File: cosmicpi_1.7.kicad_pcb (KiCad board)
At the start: 4 copper layers, 128 x 184 mm, 231 parts, among them J1 Barrel_Jack_Switch, J10 Conn_01x02_Female, J11 Conn_01x02_Male, J12 Conn_01x02_Male, J13 Conn_01x02_Female, J14 Conn_01x02_Male, J15 Conn_01x02_Female, J2 SMA, J3 USB_B_Micro, J4 Conn_01x04_Male, J5 Conn_01x04_Male, J6 SWD, J7 Raspberry_Pi_2_3, J8 Conn_01x02_Male, J9 Conn_01x02_Female, Q1 BSS123, Q2 BSS123, U1 MCP47CMB22, U10 TPS62163DSG, U11 LM555, U12 LM555, U13 LP2985-3.3, U14 AD8039, U15 AD8039, U16 LP2985-3.3, U17 MAX1932, U18 MAX1932, U19 AD8039, U2 STM32F401RETx, U3 L76-M33, U4 74HC00, U5 BME280, U5 LPS25HB, U6 LM555, U7 LSM9DS1, U8 SI7006-A20, U9 MAX991, Y1 8 MHz

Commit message: updated a little
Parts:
- removed the REF** at (103.0, 56.0)
- removed the REF** at (56.5, 30.0)
- removed the REF** at (20.2, 69.2)
- removed the REF** at (100.0, 91.2)
- removed the REF** at (78.8, 119.2)
- removed the REF** at (70.0, 99.8)
- removed the REF** at (20.5, 156.0)
- removed the REF** at (141.2, 109.2)
- removed the REF** at (128.5, 118.5)
- removed the REF** at (44.2, 26.0)
- removed the REF** at (139.8, 39.0)
- removed the REF** at (103.0, 167.0)
- removed the REF** at (82.8, 55.0)
- removed the REF** at (46.8, 54.0)
- removed the REF** at (18.8, 20.2)
- removed the REF** at (100.0, 75.5)
- removed the REF** at (100.0, 144.5)
- removed the REF** at (46.8, 75.5)
- removed the REF** at (33.8, 75.5)
- removed the REF** at (85.5, 168.5)
- removed the REF** at (57.5, 168.5)
- removed the U5 at (49.5, 23.0)
- added C100: 10u, Capacitor_SMD:C_1206_3216Metric, F.Cu at (-70.3, 109.9)
- added C101: 10u, Capacitor_SMD:C_1206_3216Metric, F.Cu at (-47.9, 90.2)
- added C102: 10u, Capacitor_SMD:C_1206_3216Metric, F.Cu at (-64.7, 106.7)
- added C103: 10u, Capacitor_SMD:C_1206_3216Metric, F.Cu at (-59.1, 100.1)
- added C104: 10u, Capacitor_SMD:C_1206_3216Metric, F.Cu at (-53.5, 96.8)
- added C105: 10u, Capacitor_SMD:C_1206_3216Metric, F.Cu at (-47.9, 93.5)
- added C106: 10u, Capacitor_SMD:C_1206_3216Metric, F.Cu at (-59.1, 103.4)
- added C107: 10u, Capacitor_SMD:C_1206_3216Metric, F.Cu at (-64.7, 109.9)
- added C108: 10u, Capacitor_SMD:C_1206_3216Metric, F.Cu at (-42.3, 90.2)
- added C109: 10u, Capacitor_SMD:C_1206_3216Metric, F.Cu at (-59.1, 106.7)
- added C110: 10u, Capacitor_SMD:C_1206_3216Metric, F.Cu at (-53.5, 100.1)
- added C111: 10n, Capacitor_SMD:C_1206_3216Metric, F.Cu at (-42.3, 93.5)
- added C77: 4.3p, Capacitor_SMD:C_0603_1608Metric, F.Cu at (-37.3, 64.8)
- added C78: 4.3p, Capacitor_SMD:C_0603_1608Metric, F.Cu at (-43.9, 66.5)
- added C79: 100n, Capacitor_SMD:C_0603_1608Metric, F.Cu at (-48.0, 71.0)
- added C80: 10u, Capacitor_SMD:C_1206_3216Metric, F.Cu at (-59.1, 109.9)
- added C81: 10u, Capacitor_SMD:C_1206_3216Metric, F.Cu at (-53.5, 103.4)
- added C82: 10u, Capacitor_SMD:C_1206_3216Metric, F.Cu at (-36.7, 90.2)
- added C83: 10u, Capacitor_SMD:C_1206_3216Metric, F.Cu at (-59.1, 96.8)
- added C84: 10u, Capacitor_SMD:C_1206_3216Metric, F.Cu at (-53.5, 93.5)
- added C85: 10u, Capacitor_SMD:C_1206_3216Metric, F.Cu at (-70.3, 93.5)
- added C86: 10u, Capacitor_SMD:C_1206_3216Metric, F.Cu at (-64.7, 90.2)
- added C87: 10u, Capacitor_SMD:C_1206_3216Metric, F.Cu at (-70.3, 96.8)
- added C88: 10u, Capacitor_SMD:C_1206_3216Metric, F.Cu at (-64.7, 93.5)
- added C89: 10u, Capacitor_SMD:C_1206_3216Metric, F.Cu at (-59.1, 90.2)
- added C90: 10u, Capacitor_SMD:C_1206_3216Metric, F.Cu at (-70.3, 100.1)
- added C91: 10u, Capacitor_SMD:C_1206_3216Metric, F.Cu at (-64.7, 96.8)
- added C92: 10u, Capacitor_SMD:C_1206_3216Metric, F.Cu at (-59.1, 93.5)
- added C93: 10u, Capacitor_SMD:C_1206_3216Metric, F.Cu at (-70.3, 103.4)
- added C94: 10u, Capacitor_SMD:C_1206_3216Metric, F.Cu at (-53.5, 90.2)
- added C95: 10n, Capacitor_SMD:C_1206_3216Metric, F.Cu at (-70.3, 106.7)
- added C96: 10u, Capacitor_SMD:C_1206_3216Metric, F.Cu at (-64.7, 100.1)
- added C97: 10u, Capacitor_SMD:C_1206_3216Metric, F.Cu at (-47.9, 96.8)
- added C98: 10u, Capacitor_SMD:C_1206_3216Metric, F.Cu at (-70.3, 90.2)
- added C99: 10u, Capacitor_SMD:C_1206_3216Metric, F.Cu at (-64.7, 103.4)
- added D10: B140, Diode_SMD:D_SMA, F.Cu at (-50.0, 67.5)
- added D11: BAT54SW, Package_TO_SOT_SMD:SOT-323_SC-70, F.Cu at (-37.3, 93.7)
- added D12: BAT54SW, Package_TO_SOT_SMD:SOT-323_SC-70, F.Cu at (-48.5, 104.8)
- added D13: BAT54SW, Package_TO_SOT_SMD:SOT-323_SC-70, F.Cu at (-31.6, 90.4)
- added D14: BAT54SW, Package_TO_SOT_SMD:SOT-323_SC-70, F.Cu at (-44.0, 100.6)
- added D15: BAT54SW, Package_TO_SOT_SMD:SOT-323_SC-70, F.Cu at (-54.1, 111.4)
- added D16: BAT54SW, Package_TO_SOT_SMD:SOT-323_SC-70, F.Cu at (-38.4, 97.3)
- added D17: BAT54SW, Package_TO_SOT_SMD:SOT-323_SC-70, F.Cu at (-49.6, 108.5)
- added D18: BAT54SW, Package_TO_SOT_SMD:SOT-323_SC-70, F.Cu at (-44.0, 104.3)
- added D19: BAT54SW, Package_TO_SOT_SMD:SOT-323_SC-70, F.Cu at (-32.8, 94.0)
- added D20: BAT54SW, Package_TO_SOT_SMD:SOT-323_SC-70, F.Cu at (-42.9, 97.0)
- added D21: BAT54SW, Package_TO_SOT_SMD:SOT-323_SC-70, F.Cu at (-39.6, 101.0)
- added D22: BAT54SW, Package_TO_SOT_SMD:SOT-323_SC-70, F.Cu at (-45.2, 108.5)
- added D23: BAT54SW, Package_TO_SOT_SMD:SOT-323_SC-70, F.Cu at (-34.0, 97.7)
- added D24: BAT54SW, Package_TO_SOT_SMD:SOT-323_SC-70, F.Cu at (-39.6, 104.6)
- added D9: B140, Diode_SMD:D_SMA, F.Cu at (-35.3, 61.2)
- added Q3: BSS123, Package_TO_SOT_SMD:SOT-23, F.Cu at (-48.5, 100.7)
- added Q4: BSS123, Package_TO_SOT_SMD:SOT-23, F.Cu at (-54.1, 107.3)
- added R71: 100k, Resistor_SMD:R_0603_1608Metric, F.Cu at (-52.0, 71.0)
- added R72: 10k, Resistor_SMD:R_0603_1608Metric, F.Cu at (-41.0, 107.7)
- added R73: 180, Resistor_SMD:R_0603_1608Metric, F.Cu at (-35.3, 100.8)
- added R74: 10k, Resistor_SMD:R_0603_1608Metric, F.Cu at (-41.8, 111.5)
- added R75: 10k, Resistor_SMD:R_0603_1608Metric, F.Cu at (-49.9, 111.5)
- added R76: 180, Resistor_SMD:R_0603_1608Metric, F.Cu at (-45.8, 111.5)
- added R77: 10k, Resistor_SMD:R_0603_1608Metric, F.Cu at (-35.3, 103.3)
- added Y2: 32.768KHz, Crystal:Crystal_SMD_HC49-SD, F.Cu at (-46.7, 62.1)
- C56: value 10u -> 470u; footprint Capacitor_SMD:C_0603_1608Metric -> Capacitor_SMD:C_Elec_10x10.2
- U8: value SI7006-A20 -> ESP-12F; footprint Package_DFN_QFN:DFN-6-1EP_3x3mm_P1mm_EP1.5x2.4mm -> RF_Module:ESP-12E
- moved U8 177.6 mm to (109.2, 185.4), turned to 180 degrees
- moved J7 146.4 mm to (69.8, 172.7)
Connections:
- C43 pad 1: V_OFFSET -> GNDREF
- C43 pad 2: GNDREF -> V_OFFSET
- C44 pad 1: V_OFFSET -> GNDREF
- C44 pad 2: GNDREF -> V_OFFSET
- C49 pad 1: V_OFFSET -> GNDREF
- C49 pad 2: GNDREF -> V_OFFSET
- C50 pad 1: V_OFFSET -> GNDREF
- C50 pad 2: GNDREF -> V_OFFSET
- C56 pad 1: GND -> Net-(C56-Pad1)
- C56 pad 2: Net-(C56-Pad2) -> GND
- J1 pad 1: Net-(C56-Pad2) -> Net-(D9-Pad1)
- J3 pad 1: USB_OTG_VBUS -> Net-(D10-Pad1)
- J7 pad 3: SDA_SLAVE -> ESP_Reset
- J7 pad 5: SCL_SLAVE -> ESP_Boot
- R6 pad 2: LED1 -> pwr_led
- R7 pad 2: LED2 -> evt_led
- U1 pad 6: Net-(U1-Pad6) -> GND
- U10 pad 2: Net-(C56-Pad2) -> Net-(C56-Pad1)
- U10 pad 3: Net-(C56-Pad2) -> Net-(C56-Pad1)
- U2 pad 16: Net-(U2-Pad16) -> GPSRX
- U2 pad 17: Net-(U2-Pad17) -> GPSTX
- U2 pad 20: LED1 -> BIASFB1
- U2 pad 21: LED2 -> BIASFB2
- U2 pad 23: BIASFB1 -> pwr_led
- U2 pad 26: BIASFB2 -> PSU_B_DRIVE
- U2 pad 29: TRIG_OUT -> Net-(U2-Pad29)
- U2 pad 3: ACC_INT1 -> Net-(C77-Pad1)
- U2 pad 4: ACC_INT2 -> Net-(C78-Pad1)
- U2 pad 40: MAG_INT -> Net-(U2-Pad40)
- U2 pad 41: SCL_SLAVE -> evt_led
- U2 pad 55: Net-(U2-Pad55) -> TRIG_OUT
- U2 pad 56: SDA_SLAVE -> Net-(U2-Pad56)
- U2 pad 57: Net-(U2-Pad57) -> PSU_A_DRIVE
- U2 pad 58: GPSRX -> Net-(U2-Pad58)
- U7 pad 10: MAG_INT -> Net-(U7-Pad10)
- U7 pad 11: ACC_INT2 -> Net-(U7-Pad11)
- U7 pad 12: ACC_INT1 -> Net-(U7-Pad12)
- U8 pad 1: SDA0 -> ESP_Reset
- U8 pad 2: GND -> Net-(U8-Pad2)
- U8 pad 3: Net-(U8-Pad3) -> +3V3
- U8 pad 5: +3V3 -> Net-(U8-Pad5)
- U8 pad 6: SCL0 -> Net-(U8-Pad6)
- U8 pad 7: (no net) -> Net-(U8-Pad7)
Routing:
- net +5V: track 373.2 -> 0.00 mm, vias 4 -> 0
- net _RESET: track 178.8 -> 0.00 mm, vias 2 -> 0
- net RX0: track 83.2 -> 0.00 mm, vias 2 -> 0
- net TX0: track 78.7 -> 0.00 mm, vias 2 -> 0
- net FLAG: track 48.0 -> 0.00 mm, vias 3 -> 0
- net SDA_SLAVE: track 43.2 -> 0.00 mm, vias 2 -> 0
- net BOOT0: track 40.2 -> 0.00 mm, vias 2 -> 0
- net SCL_SLAVE: track 36.5 -> 0.00 mm, vias 2 -> 0
- net Net-(U2-Pad2): track 0.00 -> 30.5 mm, vias 0 -> 2
- net BARO_INT: track 30.5 -> 0.00 mm, vias 2 -> 0
- removed copper zone on F.Cu, net (none)
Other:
- board size 128 x 184 mm -> 128 x 231.6 mm

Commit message: footprints corrected, routing in progress
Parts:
- removed C100, C101, C102, C103, C104, C105, C106, C107, C108, C109, C110, C80, C81, C82, C83, C84, C85, C86, C87, C88, C89, C90, C91, C92, C93, C94, C96, C97, C98, C99: 10u, Capacitor_SMD:C_1206_3216Metric
- removed C111, C95: 10n, Capacitor_SMD:C_1206_3216Metric
- removed D11, D12, D13, D14, D15, D16, D17, D18, D19, D20, D21, D22, D23, D24: BAT54SW, Package_TO_SOT_SMD:SOT-323_SC-70
- removed Q3, Q4: BSS123, Package_TO_SOT_SMD:SOT-23
- removed R72, R74, R75, R77: 10k, Resistor_SMD:R_0603_1608Metric
- removed R73, R76: 180, Resistor_SMD:R_0603_1608Metric
- D10, D9: value B140 -> B140-E3
- Y1: footprint Crystal:Crystal_SMD_HC49-SD -> Crystal:Crystal_SMD_5032-4Pin_5.0x3.2mm
- Y2: footprint Crystal:Crystal_SMD_HC49-SD -> Crystal:Crystal_SMD_EuroQuartz_EQ161-2Pin_3.2x1.5mm
- moved R71 206.4 mm to (121.0, 183.6), turned to 180 degrees
- moved C79 204.8 mm to (120.6, 187.4), turned to 90 degrees
- moved Y2 105.5 mm to (56.4, 39.8), turned to 270 degrees
- moved C78 100.4 mm to (53.2, 41.0), turned to 180 degrees
- moved C77 94.3 mm to (53.2, 38.4), turned to 180 degrees
- moved D10 84.8 mm to (23.6, 109.6), turned to 90 degrees
- moved D9 63.5 mm to (27.6, 70.0), turned to 180 degrees
- moved U5 37.5 mm to (35.6, 22.6)
- moved C15 21.4 mm to (32.6, 21.2)
- moved C57 11.5 mm to (35.2, 99.6)
- moved U16 10.6 mm to (29.6, 87.6)
- moved C58 10.3 mm to (32.8, 91.2)
- moved U10 9.92 mm to (32.9, 96.2)
- moved L1 8.96 mm to (36.6, 96.6)
- moved C3 8.34 mm to (53.4, 44.2)
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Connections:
- D10 pad 1: Net-(D10-Pad1) -> Net-(C56-Pad1)
- D10 pad 2: +5V -> Net-(D10-Pad2)
- D9 pad 1: Net-(D9-Pad1) -> +5V
- D9 pad 2: Net-(C56-Pad1) -> Net-(D9-Pad2)
- J1 pad 1: Net-(D9-Pad1) -> Net-(D10-Pad2)
- J3 pad 1: Net-(D10-Pad1) -> Net-(D9-Pad2)
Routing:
- net LED2: track 132.5 -> 0.00 mm, vias 2 -> 0
- net LED1: track 124.6 -> 0.00 mm, vias 2 -> 0
- net SWCLK: track 119.9 -> 0.00 mm, vias 4 -> 0
- net SWDIO: track 118.8 -> 0.00 mm, vias 3 -> 0
- net USB_OTG_DM: track 111.5 -> 0.00 mm, vias 2 -> 0
- net USB_OTG_DP: track 111.1 -> 7.95 mm, vias 3 -> 1
- net USB_OTG_VBUS: track 94.0 -> 0.00 mm, vias 2 -> 0
- net MAG_INT: track 79.6 -> 0.00 mm, vias 4 -> 0
- net HVPSU_CS2: track 59.1 -> 4.87 mm, vias 3 -> 0
- net ACC_INT2: track 45.7 -> 0.00 mm, vias 2 -> 0
- net GND: track 139.2 -> 93.8 mm, vias 135 -> 121
- net ACC_INT1: track 44.6 -> 0.00 mm, vias 2 -> 0
- net Net-(U2-Pad2): track 30.5 -> 0.00 mm, vias 2 -> 0
- net Net-(C4-Pad1): track 15.0 -> 0.00 mm
- net +3V3: track 306.3 -> 291.4 mm, vias 27 -> 28
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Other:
- board size 128 x 231.6 mm -> 128 x 184 mm
- board text added: "<- side LED orientation"
- board text removed: "SCINTILLATOR SUPPORT"

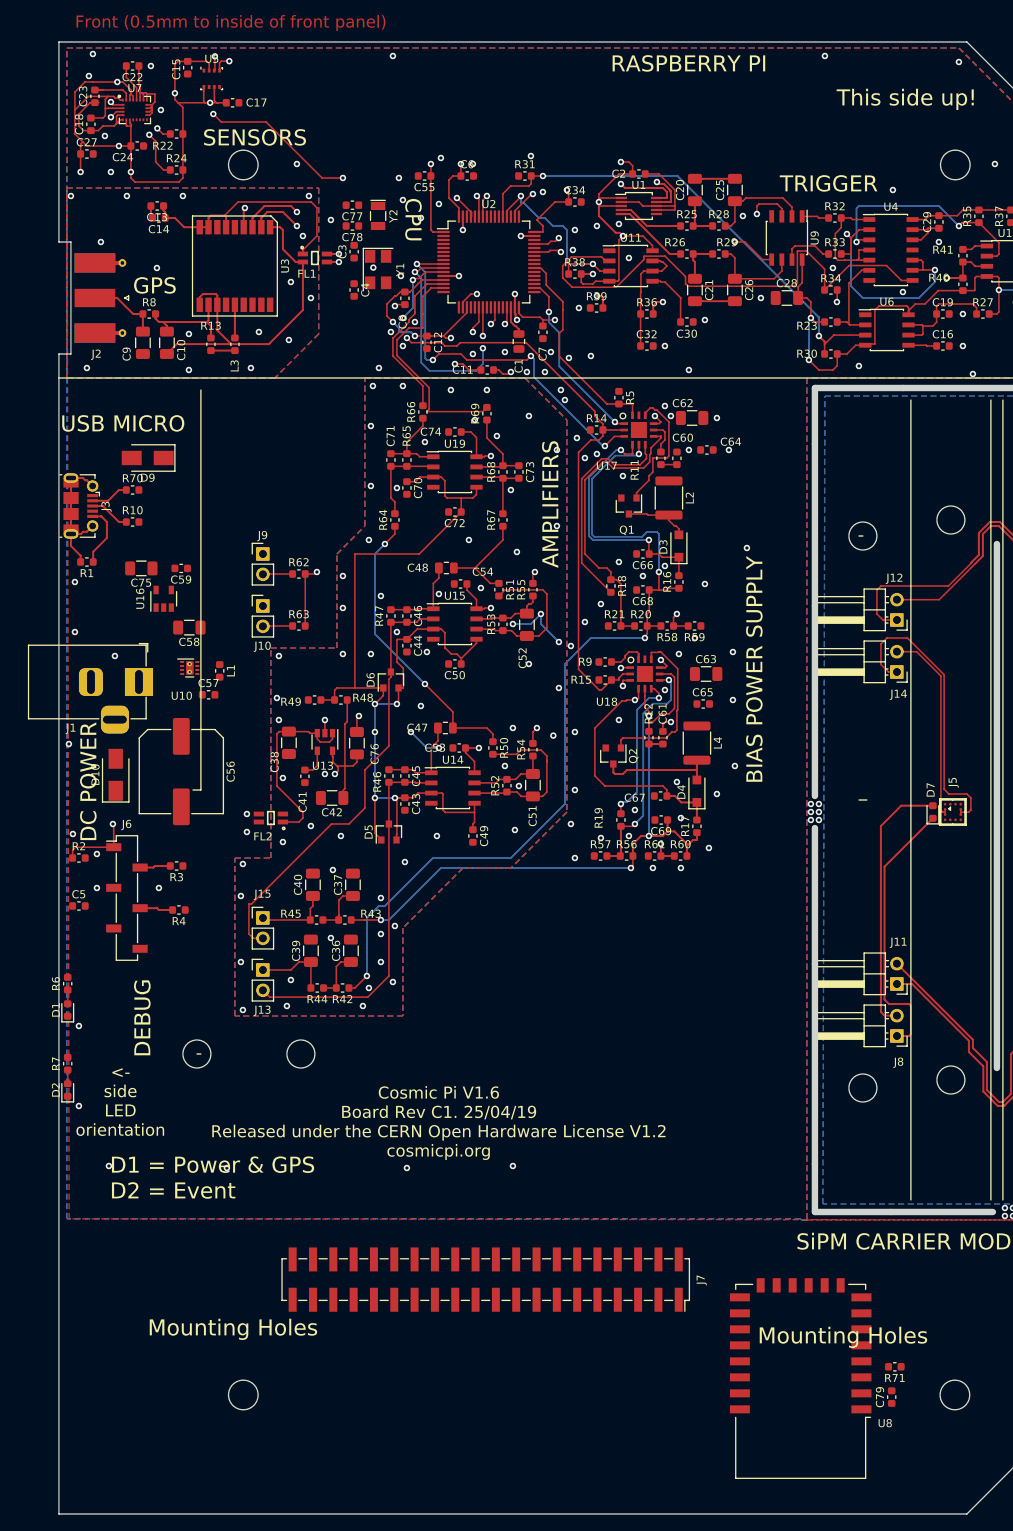
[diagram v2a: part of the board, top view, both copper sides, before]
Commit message: finished place and route
BOM still needs updating!
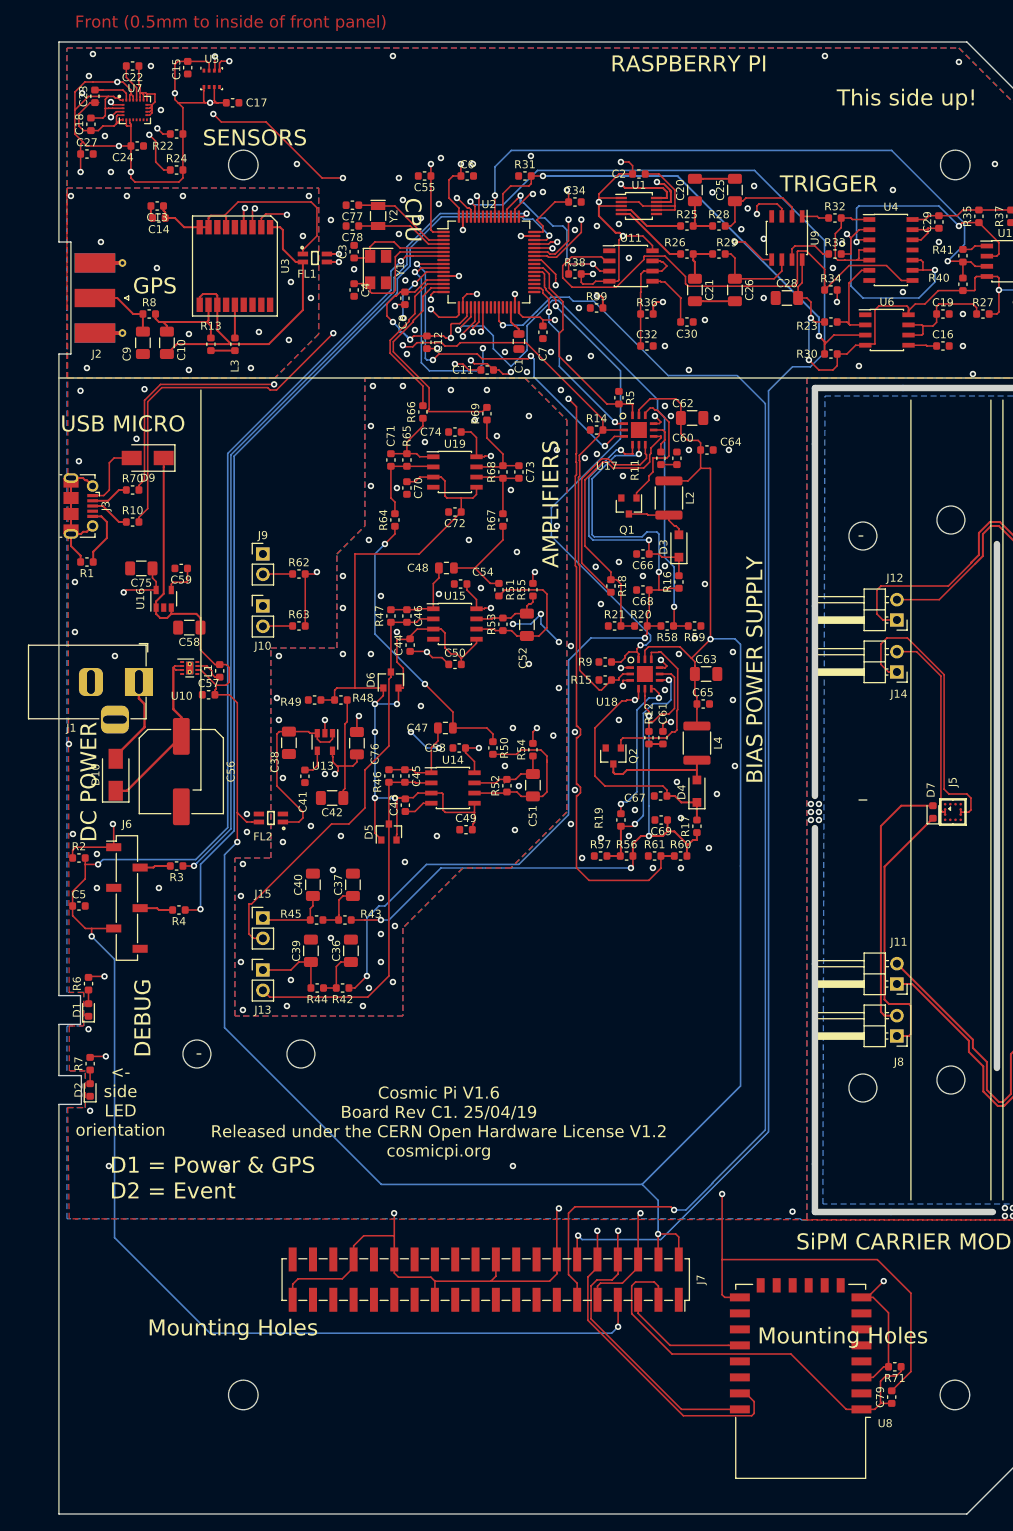
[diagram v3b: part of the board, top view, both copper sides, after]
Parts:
- moved D2 2.80 mm to (20.4, 149.0)
- moved R7 2.80 mm to (20.4, 145.7)
- moved D1 2.60 mm to (20.2, 139.0)
- moved R6 2.60 mm to (20.2, 135.7)
- moved C49 1.17 mm to (67.4, 116.5), turned to 0 degrees
- moved C44 0.41 mm to (60.4, 93.4), turned to 90 degrees
- moved C43 0.16 mm to (59.8, 113.4), turned to 90 degrees
- moved C50 0.05 mm to (66.0, 95.8), turned to 0 degrees
- turned L1 to 90 degrees
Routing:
- net +5V: track 0.00 -> 307.4 mm, vias 0 -> 3
- net _RESET: track 0.00 -> 230.5 mm, vias 0 -> 4
- net TX0: track 0.00 -> 206.3 mm, vias 0 -> 2
- net RX0: track 0.00 -> 201.9 mm, vias 0 -> 2
- net BOOT0: track 0.00 -> 200.2 mm, vias 0 -> 2
- net FLAG: track 0.00 -> 173.5 mm, vias 0 -> 2
- net evt_led: track 0.00 -> 134.6 mm, vias 0 -> 2
- net GND: track 93.8 -> 224.5 mm, vias 121 -> 129
- net pwr_led: track 0.00 -> 118.6 mm, vias 0 -> 2
- net SWDIO: track 0.00 -> 117.7 mm, vias 0 -> 2
- net SWCLK: track 0.00 -> 107.6 mm, vias 0 -> 2
- net USB_OTG_DM: track 0.00 -> 74.6 mm, vias 0 -> 2
- net USB_OTG_DP: track 7.95 -> 80.6 mm, vias 1 -> 2
- net HVPSU_CS2: track 4.87 -> 67.3 mm, vias 0 -> 2
- net ESP_Reset: track 0.00 -> 53.2 mm
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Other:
- outline, holes or cut-outs redrawn

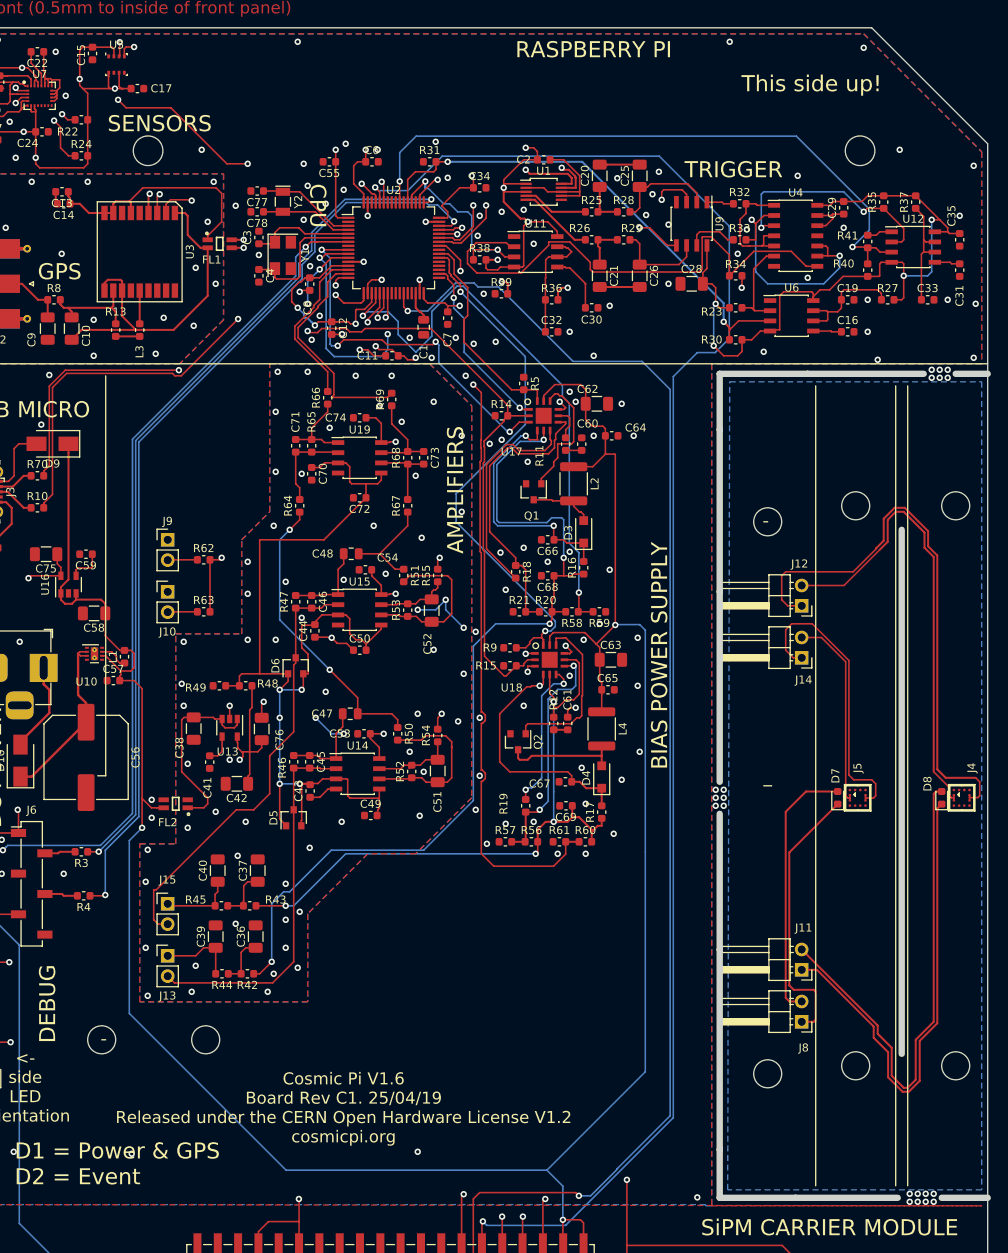
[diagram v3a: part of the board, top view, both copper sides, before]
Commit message: added BOM for 1.7
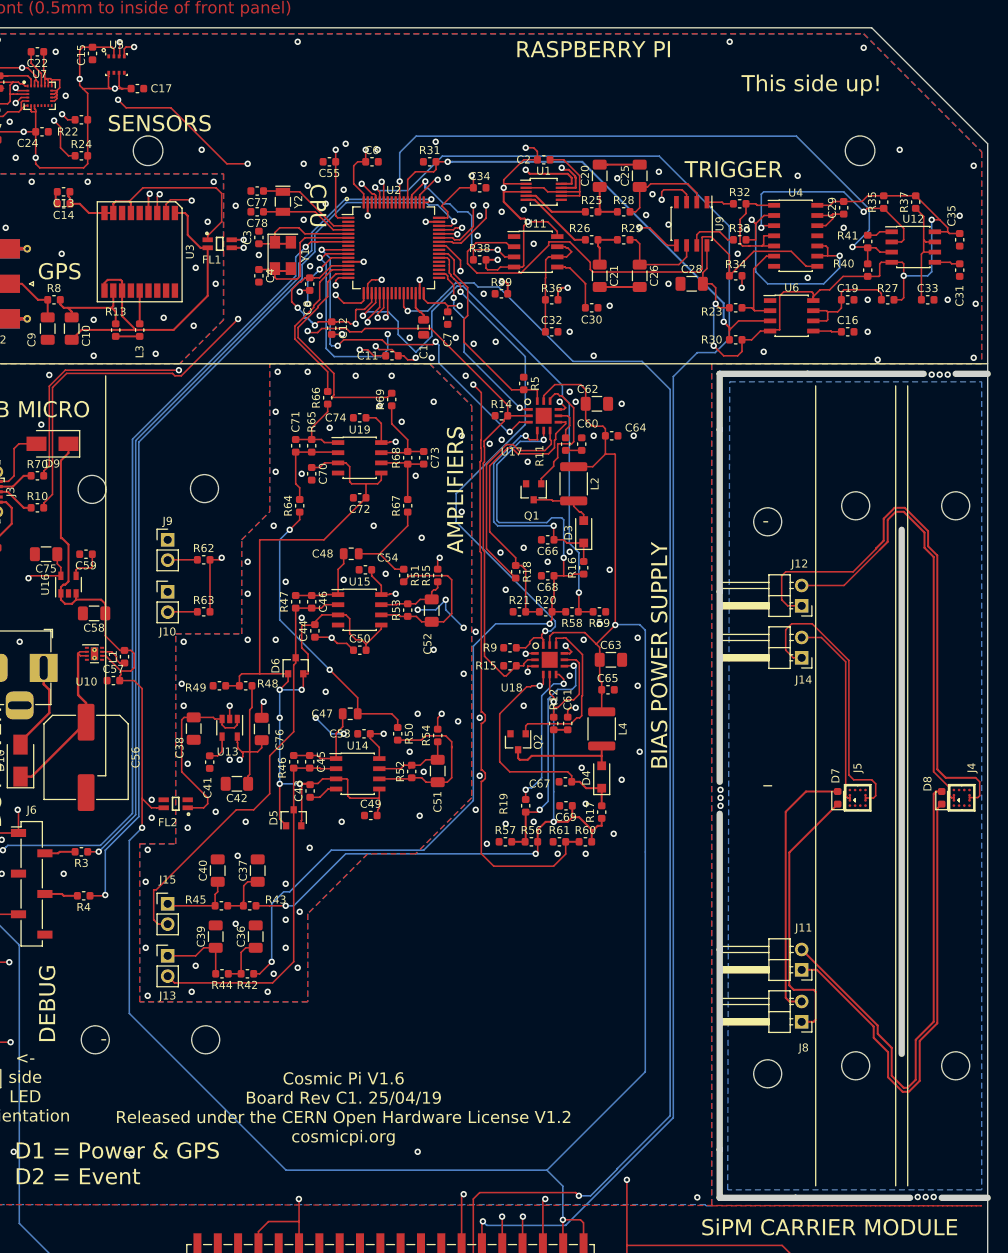
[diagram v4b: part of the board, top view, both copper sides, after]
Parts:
- added ?: , , F.Cu at (46.4, 75.6)
- added REF**: MountingHole_3.5mm, MountingHole:MountingHole_3.5mm, F.Cu at (32.5, 75.7)
- added REF**: MountingHole_3.5mm, MountingHole:MountingHole_3.5mm, F.Cu at (46.6, 75.6)
- moved REF** 0.80 mm to (33.0, 144.5)
- moved C13 0.20 mm to (29.0, 38.5)
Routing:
- net (no net): track 0.00 -> 3.60 mm, vias 20 -> 9
- net +5V: track 307.4 -> 308.4 mm
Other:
- outline, holes or cut-outs redrawn
